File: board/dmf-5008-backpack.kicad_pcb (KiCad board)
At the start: 2 copper layers, 1 part, among them P1 CONN_01X25

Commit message: Update file format to KiCAD 6
Also rescue old symbols missing or changed in the new libraries.
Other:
- net class Default removed

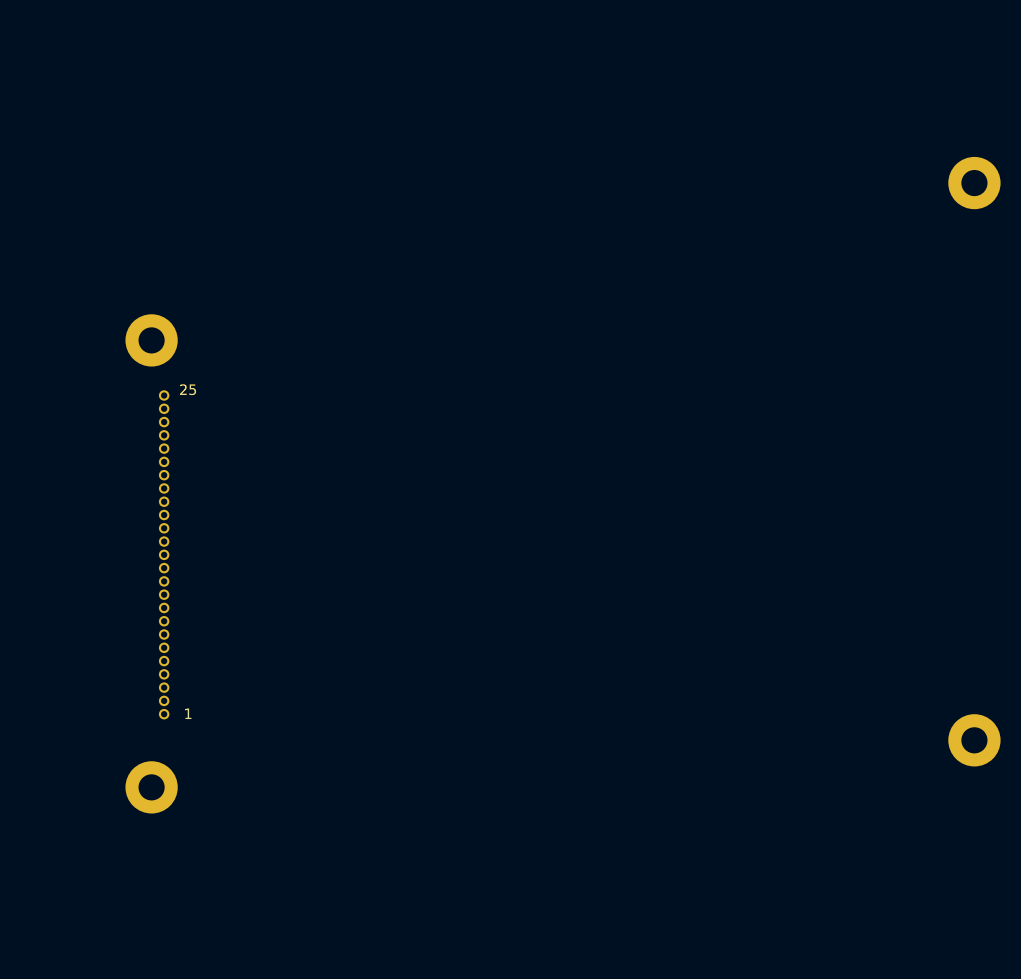
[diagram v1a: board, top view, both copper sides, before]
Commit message: Rough draft of redesign around Pi Pico
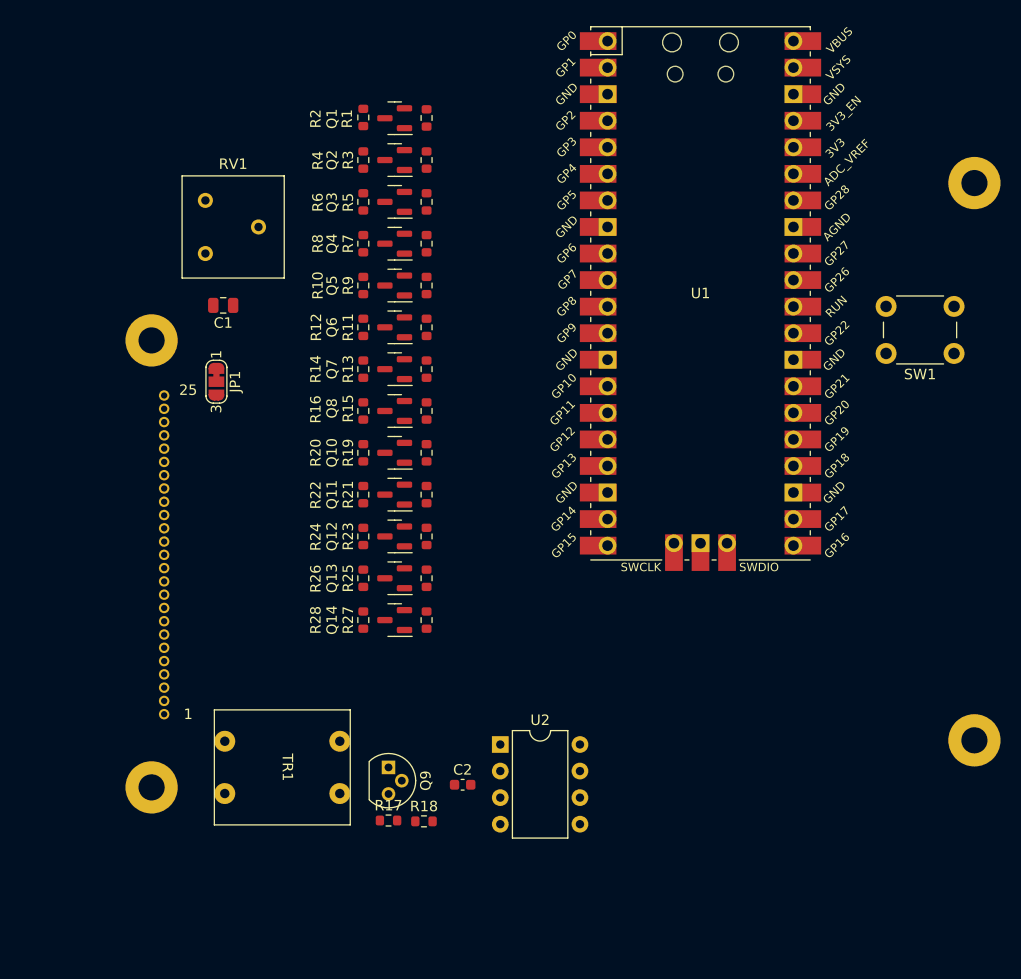
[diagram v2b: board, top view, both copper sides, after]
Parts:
- added C1: 1uF, Capacitor_SMD:C_0805_2012Metric, F.Cu at (121.3, 72.7)
- added C2: 100n, Capacitor_SMD:C_0603_1608Metric, F.Cu at (144.2, 118.5)
- added JP1: SEL1, Jumper:SolderJumper-3_P1.3mm_Bridged12_RoundedPad1.0x1.5mm_NumberLabels, F.Cu at (120.7, 80.0)
- added Q1: BSS138, Package_TO_SOT_SMD:SOT-23, F.Cu at (137.8, 54.8)
- added Q10: BSS138, Package_TO_SOT_SMD:SOT-23, F.Cu at (137.8, 86.8)
- added Q11: BSS138, Package_TO_SOT_SMD:SOT-23, F.Cu at (137.8, 90.8)
- added Q12: BSS138, Package_TO_SOT_SMD:SOT-23, F.Cu at (137.8, 94.8)
- added Q13: BSS138, Package_TO_SOT_SMD:SOT-23, F.Cu at (137.8, 98.8)
- added Q14: BSS138, Package_TO_SOT_SMD:SOT-23, F.Cu at (137.8, 102.8)
- added Q2: BSS138, Package_TO_SOT_SMD:SOT-23, F.Cu at (137.8, 58.8)
- added Q3: BSS138, Package_TO_SOT_SMD:SOT-23, F.Cu at (137.8, 62.8)
- added Q4: BSS138, Package_TO_SOT_SMD:SOT-23, F.Cu at (137.8, 66.8)
- added Q5: BSS138, Package_TO_SOT_SMD:SOT-23, F.Cu at (137.8, 70.8)
- added Q6: BSS138, Package_TO_SOT_SMD:SOT-23, F.Cu at (137.8, 74.8)
- added Q7: BSS138, Package_TO_SOT_SMD:SOT-23, F.Cu at (137.8, 78.8)
- added Q8: BSS138, Package_TO_SOT_SMD:SOT-23, F.Cu at (137.8, 82.8)
- added Q9: S8050, Package_TO_SOT_THT:TO-92, F.Cu at (137.2, 116.8)
- added R1: 10k, Resistor_SMD:R_0603_1608Metric, F.Cu at (140.8, 54.7)
- added R10: 10k, Resistor_SMD:R_0603_1608Metric, F.Cu at (134.8, 70.8)
- added R11: 10k, Resistor_SMD:R_0603_1608Metric, F.Cu at (140.8, 74.8)
- added R12: 10k, Resistor_SMD:R_0603_1608Metric, F.Cu at (134.8, 74.8)
- added R13: 10k, Resistor_SMD:R_0603_1608Metric, F.Cu at (140.8, 78.8)
- added R14: 10k, Resistor_SMD:R_0603_1608Metric, F.Cu at (134.8, 78.8)
- added R15: 10k, Resistor_SMD:R_0603_1608Metric, F.Cu at (140.8, 82.8)
- added R16: 10k, Resistor_SMD:R_0603_1608Metric, F.Cu at (134.8, 82.8)
- added R17: 1k2, Resistor_SMD:R_0603_1608Metric, F.Cu at (137.2, 121.9)
- added R18: 2k4, Resistor_SMD:R_0603_1608Metric, F.Cu at (140.6, 122.0)
- added R19: 10k, Resistor_SMD:R_0603_1608Metric, F.Cu at (140.8, 86.8)
- added R2: 10k, Resistor_SMD:R_0603_1608Metric, F.Cu at (134.8, 54.7)
- added R20: 10k, Resistor_SMD:R_0603_1608Metric, F.Cu at (134.8, 86.8)
- added R21: 10k, Resistor_SMD:R_0603_1608Metric, F.Cu at (140.8, 90.8)
- added R22: 10k, Resistor_SMD:R_0603_1608Metric, F.Cu at (134.8, 90.8)
- added R23: 10k, Resistor_SMD:R_0603_1608Metric, F.Cu at (140.8, 94.8)
- added R24: 10k, Resistor_SMD:R_0603_1608Metric, F.Cu at (134.8, 94.8)
- added R25: 10k, Resistor_SMD:R_0603_1608Metric, F.Cu at (140.8, 98.8)
- added R26: 10k, Resistor_SMD:R_0603_1608Metric, F.Cu at (134.8, 98.8)
- added R27: 10k, Resistor_SMD:R_0603_1608Metric, F.Cu at (140.8, 102.8)
- added R28: 10k, Resistor_SMD:R_0603_1608Metric, F.Cu at (134.8, 102.8)
- added R3: 10k, Resistor_SMD:R_0603_1608Metric, F.Cu at (140.8, 58.8)
- added R4: 10k, Resistor_SMD:R_0603_1608Metric, F.Cu at (134.8, 58.8)
- added R5: 10k, Resistor_SMD:R_0603_1608Metric, F.Cu at (140.8, 62.8)
- added R6: 10k, Resistor_SMD:R_0603_1608Metric, F.Cu at (134.8, 62.8)
- added R7: 10k, Resistor_SMD:R_0603_1608Metric, F.Cu at (140.8, 66.8)
- added R8: 10k, Resistor_SMD:R_0603_1608Metric, F.Cu at (134.8, 66.8)
- added R9: 10k, Resistor_SMD:R_0603_1608Metric, F.Cu at (140.8, 70.8)
- added RV1: 10k TRIM, Potentiometer_THT:Potentiometer_Bourns_3386F_Vertical, F.Cu at (119.6, 67.7)
- added SW1: RESET, Button_Switch_THT:SW_PUSH_6mm, F.Cu at (191.2, 77.2)
- added TR1: TRANSF1, EE14_xformer:EE14_XFORMER, F.Cu at (127.0, 116.8)
- added U1: Pico, rp:RPi_Pico_SMD_TH, F.Cu at (167.0, 71.5)
- added U2: NE555P, Package_DIP:DIP-8_W7.62mm, F.Cu at (147.8, 114.7)
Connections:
- P1 pad 1: Net-(P1-Pad1) -> /EL_A
- P1 pad 10: Net-(P1-Pad10) -> /V0
- P1 pad 11: Net-(P1-Pad11) -> /LCD_5V_CS
- P1 pad 12: Net-(P1-Pad12) -> +5V
- P1 pad 13: Net-(P1-Pad13) -> /LCD_5V_D7
- P1 pad 14: Net-(P1-Pad14) -> /LCD_5V_D6
- P1 pad 15: Net-(P1-Pad15) -> /LCD_5V_D5
- P1 pad 16: Net-(P1-Pad16) -> /LCD_5V_D4
- P1 pad 17: Net-(P1-Pad17) -> /LCD_5V_D3
- P1 pad 18: Net-(P1-Pad18) -> /LCD_5V_D2
- P1 pad 19: Net-(P1-Pad19) -> /LCD_5V_D1
- P1 pad 2: Net-(P1-Pad2) -> /EL_B
- P1 pad 20: Net-(P1-Pad20) -> /LCD_5V_D0
- P1 pad 21: Net-(P1-Pad21) -> /LCD_5V_RD
- P1 pad 22: Net-(P1-Pad22) -> /LCD_5V_WR
- P1 pad 23: Net-(P1-Pad23) -> /LCD_5V_A0
- P1 pad 25: Net-(P1-Pad25) -> GND
- P1 pad 3: Net-(P1-Pad3) -> +5V
- P1 pad 4: Net-(P1-Pad4) -> /LCD_5V_RES
- P1 pad 5: Net-(P1-Pad5) -> GND
- P1 pad 6: Net-(P1-Pad6) -> GND
- P1 pad 7: Net-(P1-Pad7) -> GND
- P1 pad 8: Net-(P1-Pad8) -> +5V
- P1 pad 9: Net-(P1-Pad9) -> GND

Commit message: Update xformer and lcd footprints, add 3d models
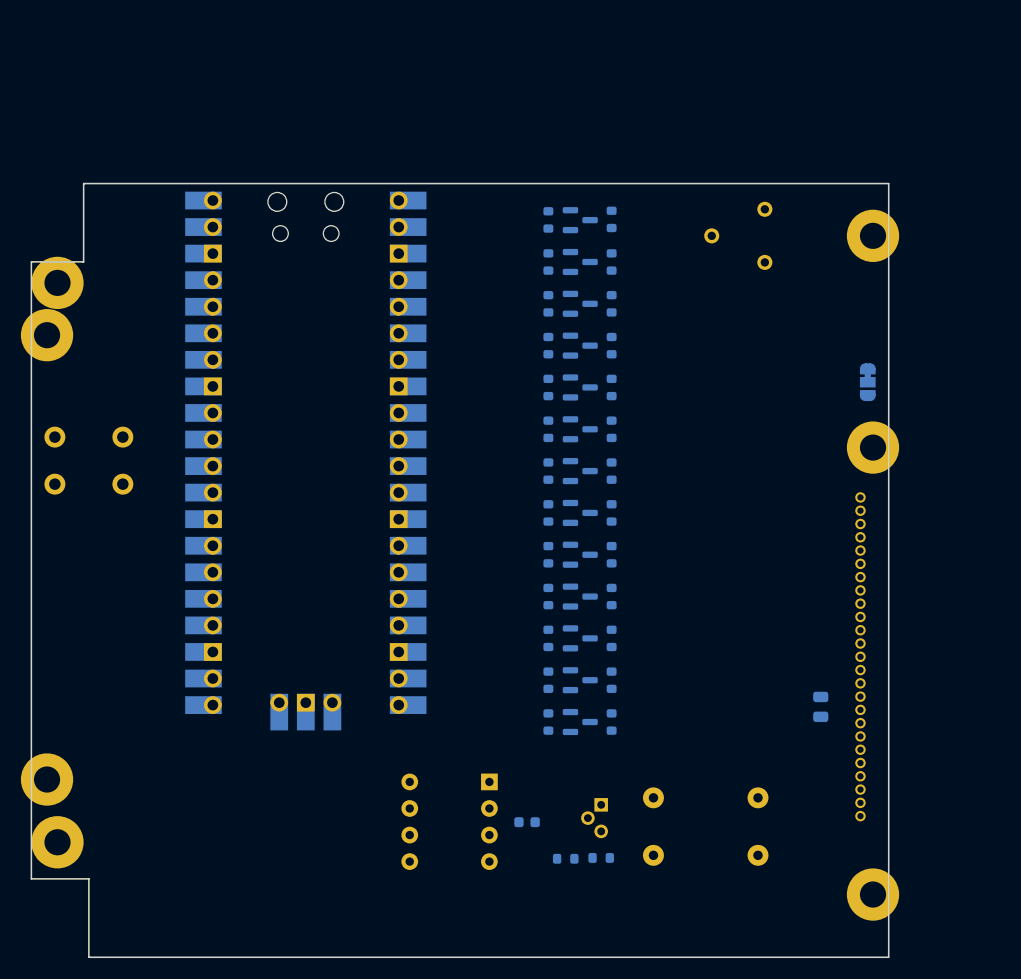
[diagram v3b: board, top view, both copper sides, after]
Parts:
- C1, C2, JP1, P1, Q1, Q10, Q11, Q12, Q13, Q14, Q2, Q3, Q4, Q5, Q6, Q7, Q8, Q9, R1, R10, R11, R12, R13, R14, R15, R16, R17, R18, R19, R2, R20, R21, R22, R23, R24, R25, R26, R27, R28, R3, R4, R5, R6, R7, R8, R9, RV1, SW1, TR1, U1, U2: moved to B.Cu
- moved SW1 86.9 mm to (105.2, 89.8), turned to 0 degrees
- moved P1 72.7 mm to (185.0, 135.0), turned to 180 degrees
- moved C1 68.9 mm to (178.5, 111.0), turned to -90 degrees
- moved JP1 62.3 mm to (183.0, 80.0)
- moved RV1 53.5 mm to (173.2, 68.5), turned to 180 degrees
- moved TR1 40.9 mm to (167.5, 122.5)
- moved U1 40.7 mm to (129.2, 86.8), turned to 180 degrees
- moved R10 25.7 mm to (158.5, 80.5)
- moved R12 25.7 mm to (158.5, 84.5)
- moved R14 25.7 mm to (158.5, 88.5)
- moved R16 25.7 mm to (158.5, 92.5)
- moved R2 25.7 mm to (158.5, 64.4)
- moved R20 25.7 mm to (158.5, 96.5)
- moved R22 25.7 mm to (158.5, 100.5)
- moved R24 25.7 mm to (158.5, 104.5)
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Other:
- board outline added: 82 x 74 mm

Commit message: Work on placement a bit
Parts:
- removed Q9: S8050, Package_TO_SOT_THT:TO-92
- removed TR1: TRANSF1, EE14_xformer:EE14_XFORMER
- added C3: 2.7n C0G 200V, Capacitor_SMD:C_0805_2012Metric_Pad1.18x1.45mm_HandSolder, B.Cu at (164.4, 118.8)
- added D1: BAS20, Package_TO_SOT_SMD:SOT-23, B.Cu at (168.7, 119.0)
- added J1: 5V IN, Connector_PinHeader_2.54mm:PinHeader_1x02_P2.54mm_Vertical, B.Cu at (155.6, 132.8)
- added J2: 3V3 IN, Connector_PinHeader_2.54mm:PinHeader_1x02_P2.54mm_Vertical, B.Cu at (164.0, 132.8)
- added J3: BOOST, Connector_PinHeader_2.54mm:PinHeader_1x03_P2.54mm_Vertical, B.Cu at (148.2, 116.8)
- added J4: Barrel_Jack_Switch, Connector_BarrelJack:BarrelJack_Horizontal, B.Cu at (130.4, 123.8)
- added R29: 0R, Resistor_SMD:R_1206_3216Metric_Pad1.30x1.75mm_HandSolder, B.Cu at (176.6, 122.6)
- added R30: 0R, Resistor_SMD:R_1206_3216Metric_Pad1.30x1.75mm_HandSolder, B.Cu at (176.6, 120.2)
- C2: value 100n -> 2u2; footprint Capacitor_SMD:C_0603_1608Metric -> Capacitor_SMD:C_0805_2012Metric
- R17: value 1k2 -> 680k
- R18: value 2k4 -> 330k
- U2: value NE555P -> MIC4830; footprint Package_DIP:DIP-8_W7.62mm -> Package_SO:MSOP-8_3x3mm_P0.65mm
- moved U2 20.2 mm to (166.4, 123.2), turned to 0 degrees
- moved C2 15.3 mm to (165.1, 126.6), turned to 0 degrees
- moved R18 4.29 mm to (158.2, 124.2)
- moved R17 2.98 mm to (158.2, 122.6)
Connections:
- net Net-(SW1-Pad2) renamed /RUN
- C2 pad 1: Net-(C2-Pad1) -> +5V
- R17 pad 2: Net-(Q9-Pad2) -> +5V
- R18 pad 1: Net-(R17-Pad1) -> Net-(R18-Pad1)
- R18 pad 2: Net-(C2-Pad1) -> /EL_ENABLE
- U2 pad 1: GND -> +5V
- U2 pad 2: Net-(C2-Pad1) -> Net-(R18-Pad1)
- U2 pad 4: /EL_ENABLE -> GND
- U2 pad 5: unconnected-(U2-Pad5) -> Net-(D1-Pad1)
- U2 pad 6: Net-(C2-Pad1) -> Net-(C3-Pad1)
- U2 pad 7: unconnected-(U2-Pad7) -> Net-(R30-Pad1)
- U2 pad 8: +5V -> Net-(R29-Pad1)
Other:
- board text added: "5V GND 3V3"

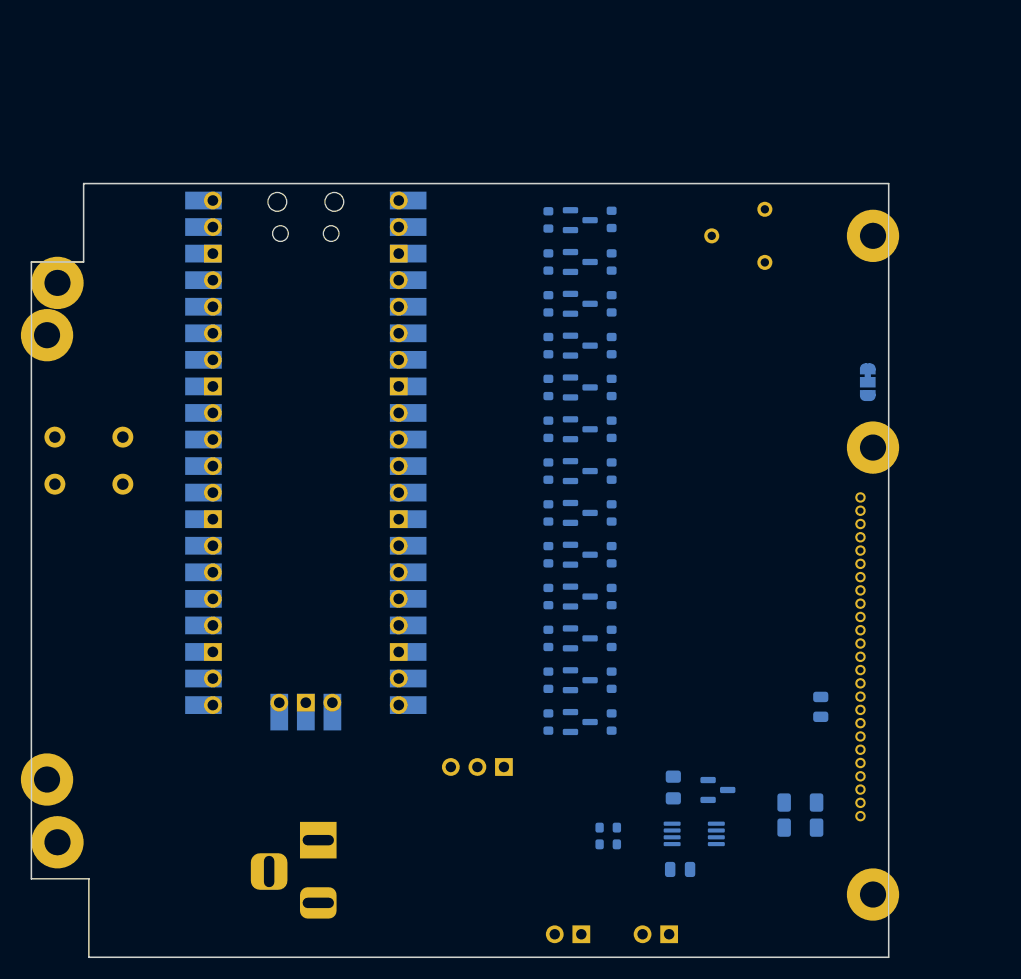
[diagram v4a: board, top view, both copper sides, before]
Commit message: Finish schematic, setup board capabilities
* Finish schematic to checklist, happy with ERC
    * Add data connections and I2C pullups
    * Make EL_ENABLE an NPN pulldown, otherwise things will be confusing
      if R_SW is only pulled up to 3v3 by a GPIO.
    * Choose an inductor for the EL driver
* Rough final placement of PCB
* Setup PCB capabilities/tracks/vias to JLC's numbers
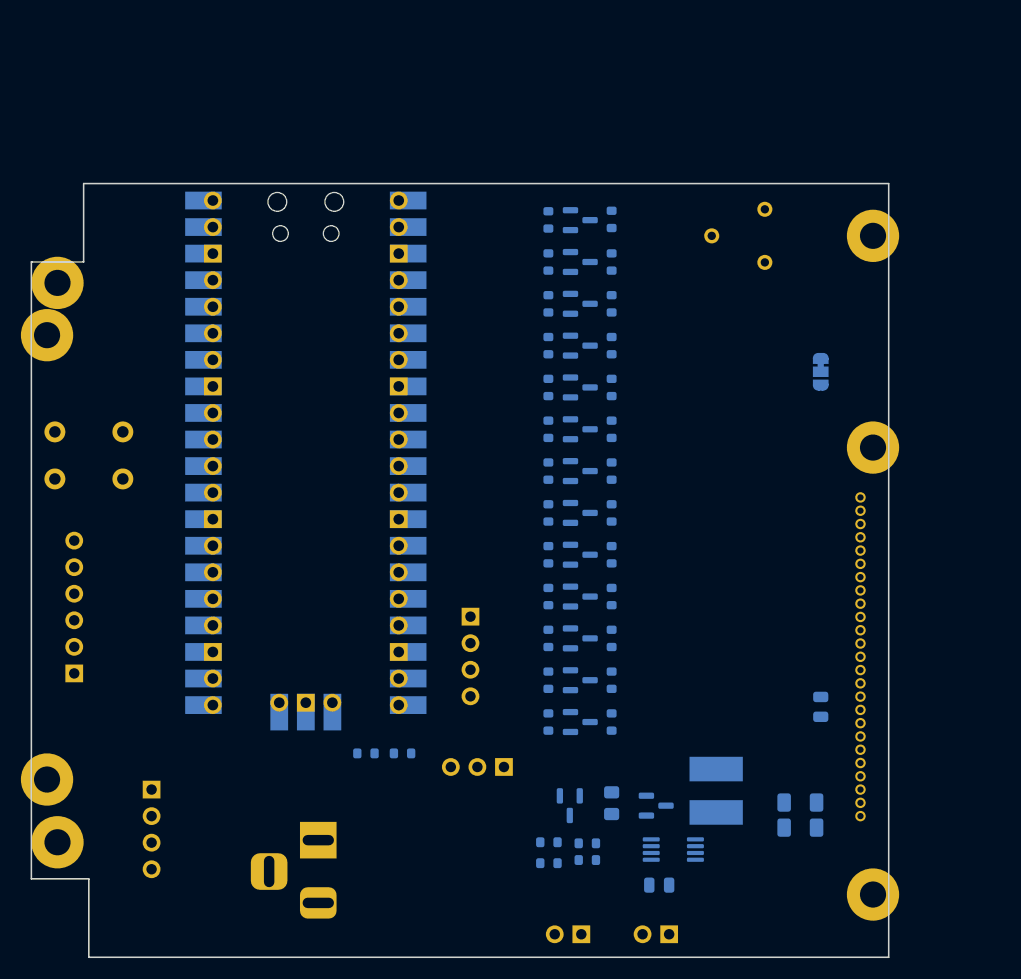
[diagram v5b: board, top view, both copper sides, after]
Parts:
- added J5: CONN_SPI, Connector_PinHeader_2.54mm:PinHeader_1x06_P2.54mm_Vertical, B.Cu at (107.1, 107.8)
- added J6: CONN_I2C, Connector_PinHeader_2.54mm:PinHeader_1x04_P2.54mm_Vertical, B.Cu at (145.0, 102.4)
- added J7: CONN_UART, Connector_PinHeader_2.54mm:PinHeader_1x04_P2.54mm_Vertical, B.Cu at (114.5, 119.0)
- added L1: Bourns SDR0604-221KL, Inductor_SMD:L_Bourns_SRN6045TA, B.Cu at (168.5, 119.1)
- added Q9: BSS138, Package_TO_SOT_SMD:SOT-23, B.Cu at (154.5, 120.5)
- added R31: 10k, Resistor_SMD:R_0603_1608Metric, B.Cu at (135.0, 115.5)
- added R32: 10k, Resistor_SMD:R_0603_1608Metric, B.Cu at (138.5, 115.5)
- added R33: 10k, Resistor_SMD:R_0603_1608Metric, B.Cu at (152.5, 124.0)
- added R34: 1k, Resistor_SMD:R_0603_1608Metric, B.Cu at (152.5, 126.0)
- moved C3 6.09 mm to (158.5, 120.3)
- moved D1 6.09 mm to (162.8, 120.5)
- moved JP1 4.61 mm to (178.5, 79.0)
- moved C2 2.50 mm to (163.1, 128.1)
- moved R17 2.50 mm to (156.2, 124.1)
- moved R18 2.50 mm to (156.2, 125.7)
- moved U2 2.50 mm to (164.4, 124.7)
- moved SW1 0.50 mm to (105.2, 89.2)
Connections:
- R18 pad 1: Net-(R18-Pad1) -> +5V
- R18 pad 2: /EL_ENABLE -> Net-(Q9-Pad3)
- U2 pad 2: Net-(R18-Pad1) -> Net-(Q9-Pad3)
